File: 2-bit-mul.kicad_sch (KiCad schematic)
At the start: 3 parts, among them U6 74LS08, U7 74LS08, U8 74HC86

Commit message: feat(mul): clean version
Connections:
- net OUT_MUL_4 is gone; now on net OUT_MUL_3: U7.6
- net OUT_MUL_1: now also U8.3; no longer U6.6
- net OUT_MUL_2: now also U8.6; no longer U8.3
- net OUT_MUL_3: no longer U8.6
- removed net IN_A: U6.1, U6.10, U6.12, U6.13, U6.2, U6.4, U6.5, U6.9
- new net IN_A0: U6.1, U6.4
- new net IN_A1: U6.12, U6.9
- new net IN_B0: U6.13, U6.2
- new net IN_B1: U6.10, U6.5
- new net OUT_MUL_0: U6.6
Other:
- moved on the sheet: U6E, U7E, U8E
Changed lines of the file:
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@@
 		)
 	)
-	(hierarchical_label "OUT_MUL_3"
+	(hierarchical_label "OUT_MUL_2"
 		(shape output)
 		(at 132.08 73.66 0)
@@
 		)
 	)
-	(hierarchical_label "IN_A"
+	(hierarchical_label "IN_B0"
 		(shape input)
 		(at 53.34 99.06 180)
@@
 		)
 	)
-	(hierarchical_label "IN_A"
+	(hierarchical_label "IN_A0"
 		(shape input)
 		(at 54.61 40.64 180)
@@
 		)
 	)
-	(hierarchical_label "IN_A"
+	(hierarchical_label "IN_A1"
 		(shape input)
 		(at 54.61 46.99 180)
@@
 		)
 	)
-	(hierarchical_label "OUT_MUL_1"
+	(hierarchical_label "OUT_MUL_0"
 		(shape output)
 		(at 132.08 53.34 0)
@@
 		)
 	)
-	(hierarchical_label "OUT_MUL_2"
+	(hierarchical_label "OUT_MUL_1"
 		(shape output)
 		(at 132.08 63.5 0)
@@
 		)
 	)
-	(hierarchical_label "IN_A"
+	(hierarchical_label "IN_B1"
 		(shape input)
 		(at 53.34 87.63 180)
@@
 		)
 	)
-	(hierarchical_label "OUT_MUL_4"
+	(hierarchical_label "OUT_MUL_3"
 		(shape output)
 		(at 132.08 87.63 0)
@@
 		(on_board yes)
 		(dnp no)
-		(fields_autoplaced yes)
 		(property "Reference" "U6"
-			(at 74.9217 87.63 0)
+			(at 74.676 101.6 0)
 			(effects
 				(font
@@
 		)
 		(property "Value" "74LS08"
-			(at 74.9217 90.17 0)
+			(at 74.93 103.886 0)
 			(effects
 				(font
@@
 	(symbol
 		(lib_id "74xx:74LS08")
-		(at 97.79 119.38 0)
+		(at 96.52 129.54 0)
 		(unit 5)
 		(exclude_from_sim no)
@@
 		(fields_autoplaced yes)
 		(property "Reference" "U7"
-			(at 104.14 118.1099 0)
+			(at 102.87 128.2699 0)
 			(effects
 				(font
@@
 		)
 		(property "Value" "74LS08"
-			(at 104.14 120.6499 0)
+			(at 102.87 130.8099 0)
 			(effects
 				(font
@@
 		)
 		(property "Footprint" ""
-			(at 97.79 119.38 0)
+			(at 96.52 129.54 0)
 			(effects
 				(font
@@
 		)
 		(property "Datasheet" "http://www.ti.com/lit/gpn/sn74LS08"
-			(at 97.79 119.38 0)
+			(at 96.52 129.54 0)
 			(effects
 				(font
@@
 		)
 		(property "Description" "Quad And2"
-			(at 97.79 119.38 0)
+			(at 96.52 129.54 0)
 			(effects
 				(font
@@
 	(symbol
 		(lib_id "74xx:74LS08")
-		(at 74.93 119.38 0)
+		(at 73.66 129.54 0)
 		(unit 5)
 		(exclude_from_sim no)
@@
 		(fields_autoplaced yes)
 		(property "Reference" "U6"
-			(at 81.28 118.1099 0)
+			(at 80.01 128.2699 0)
 			(effects
 				(font
@@
 		)
 		(property "Value" "74LS08"
-			(at 81.28 120.6499 0)
+			(at 80.01 130.8099 0)
 			(effects
 				(font
@@
 		)
 		(property "Footprint" "Package_DIP:DIP-14_W7.62mm"
-			(at 74.93 119.38 0)
+			(at 73.66 129.54 0)
 			(effects
 				(font
@@
 		)
 		(property "Datasheet" "http://www.ti.com/lit/gpn/sn74LS08"
-			(at 74.93 119.38 0)
+			(at 73.66 129.54 0)
 			(effects
 				(font
@@
 		)
 		(property "Description" "Quad And2"
-			(at 74.93 119.38 0)
+			(at 73.66 129.54 0)
 			(effects
 				(font
@@
 		(dnp no)
 		(property "Reference" "U7"
-			(at 96.774 70.612 0)
+			(at 96.52 74.168 0)
 			(effects
 				(font
@@
 	(symbol
 		(lib_id "74xx:74HC86")
-		(at 120.65 118.11 0)
+		(at 119.38 128.27 0)
 		(unit 5)
 		(exclude_from_sim no)
@@
 		(fields_autoplaced yes)
 		(property "Reference" "U8"
-			(at 127 116.8399 0)
+			(at 125.73 126.9999 0)
 			(effects
 				(font
@@
 		)
 		(property "Value" "74HC86"
-			(at 127 119.3799 0)
+			(at 125.73 129.5399 0)
 			(effects
 				(font
@@
 		)
 		(property "Footprint" ""
-			(at 120.65 118.11 0)
+			(at 119.38 128.27 0)
 			(effects
 				(font
@@
 		)
 		(property "Datasheet" "http://www.ti.com/lit/gpn/sn74HC86"
-			(at 120.65 118.11 0)
+			(at 119.38 128.27 0)
 			(effects
 				(font
@@
 		)
 		(property "Description" "Quad 2-input XOR"
-			(at 120.65 118.11 0)
-			(effects
-				(font
+			(at 119.38 128.27 0)
+			(effects
+				(font

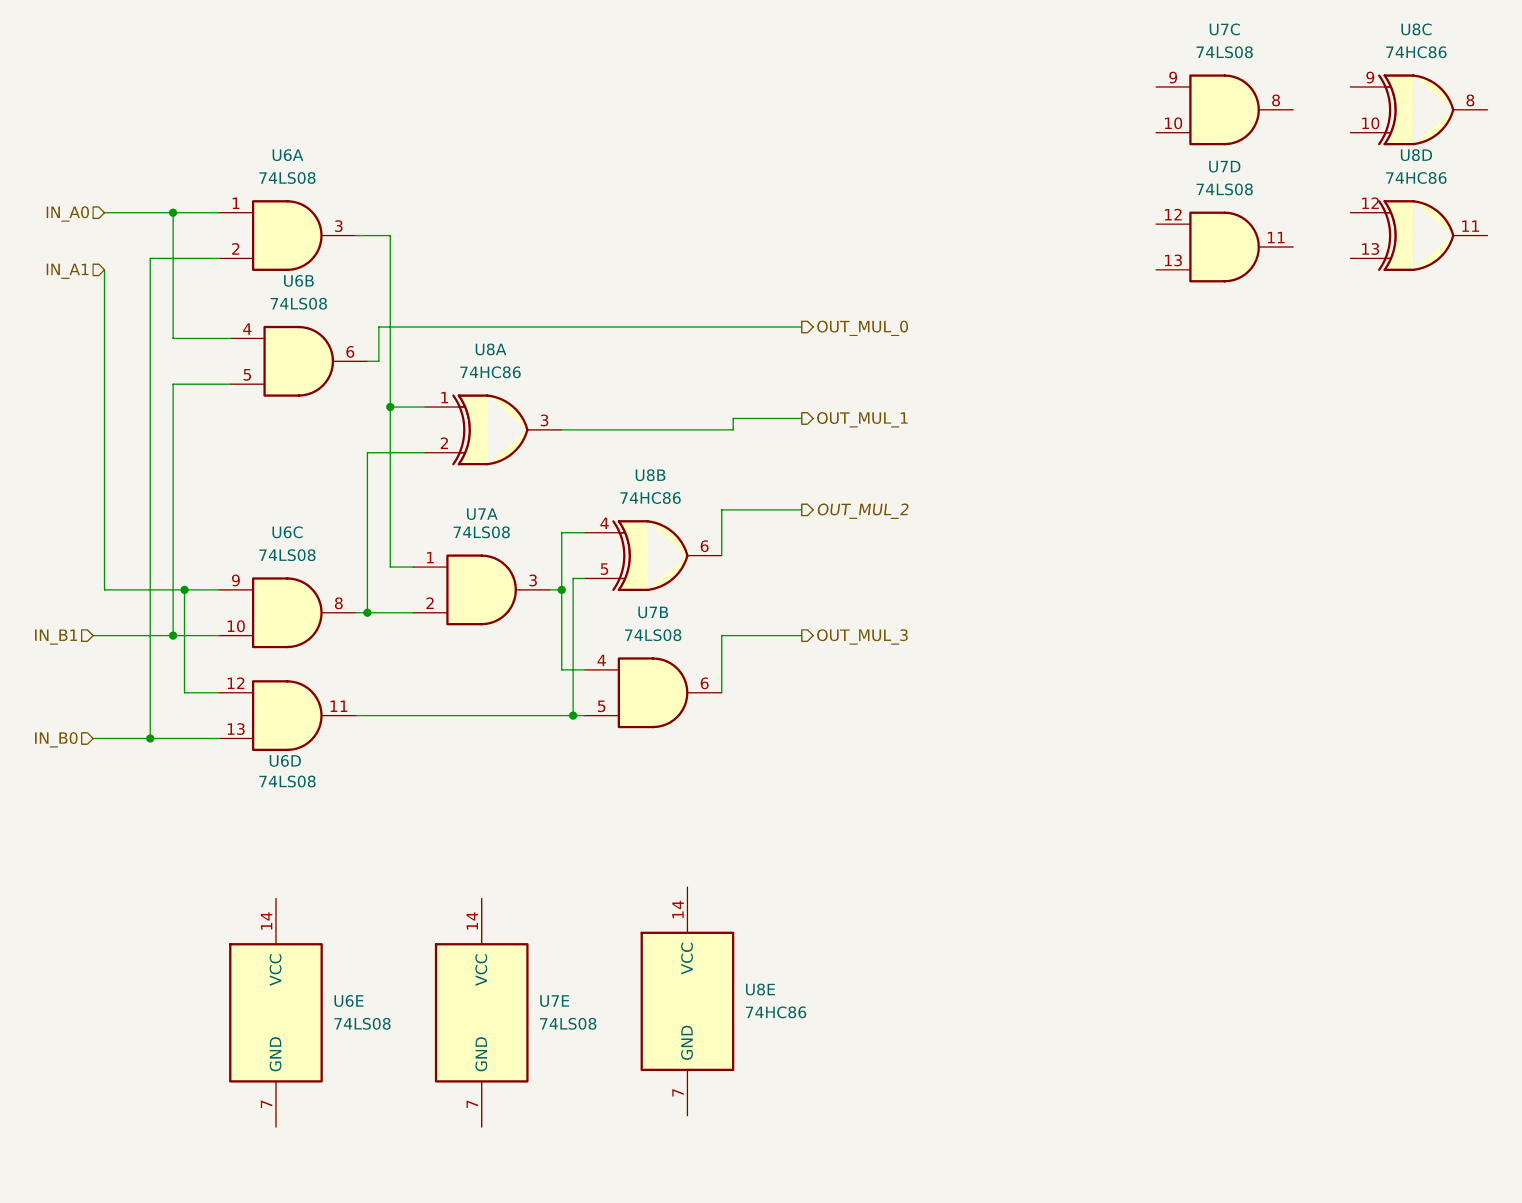
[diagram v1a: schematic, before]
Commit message: Add stuff and fix rce errors (#1)
* sync

* feat: removed ERC errors
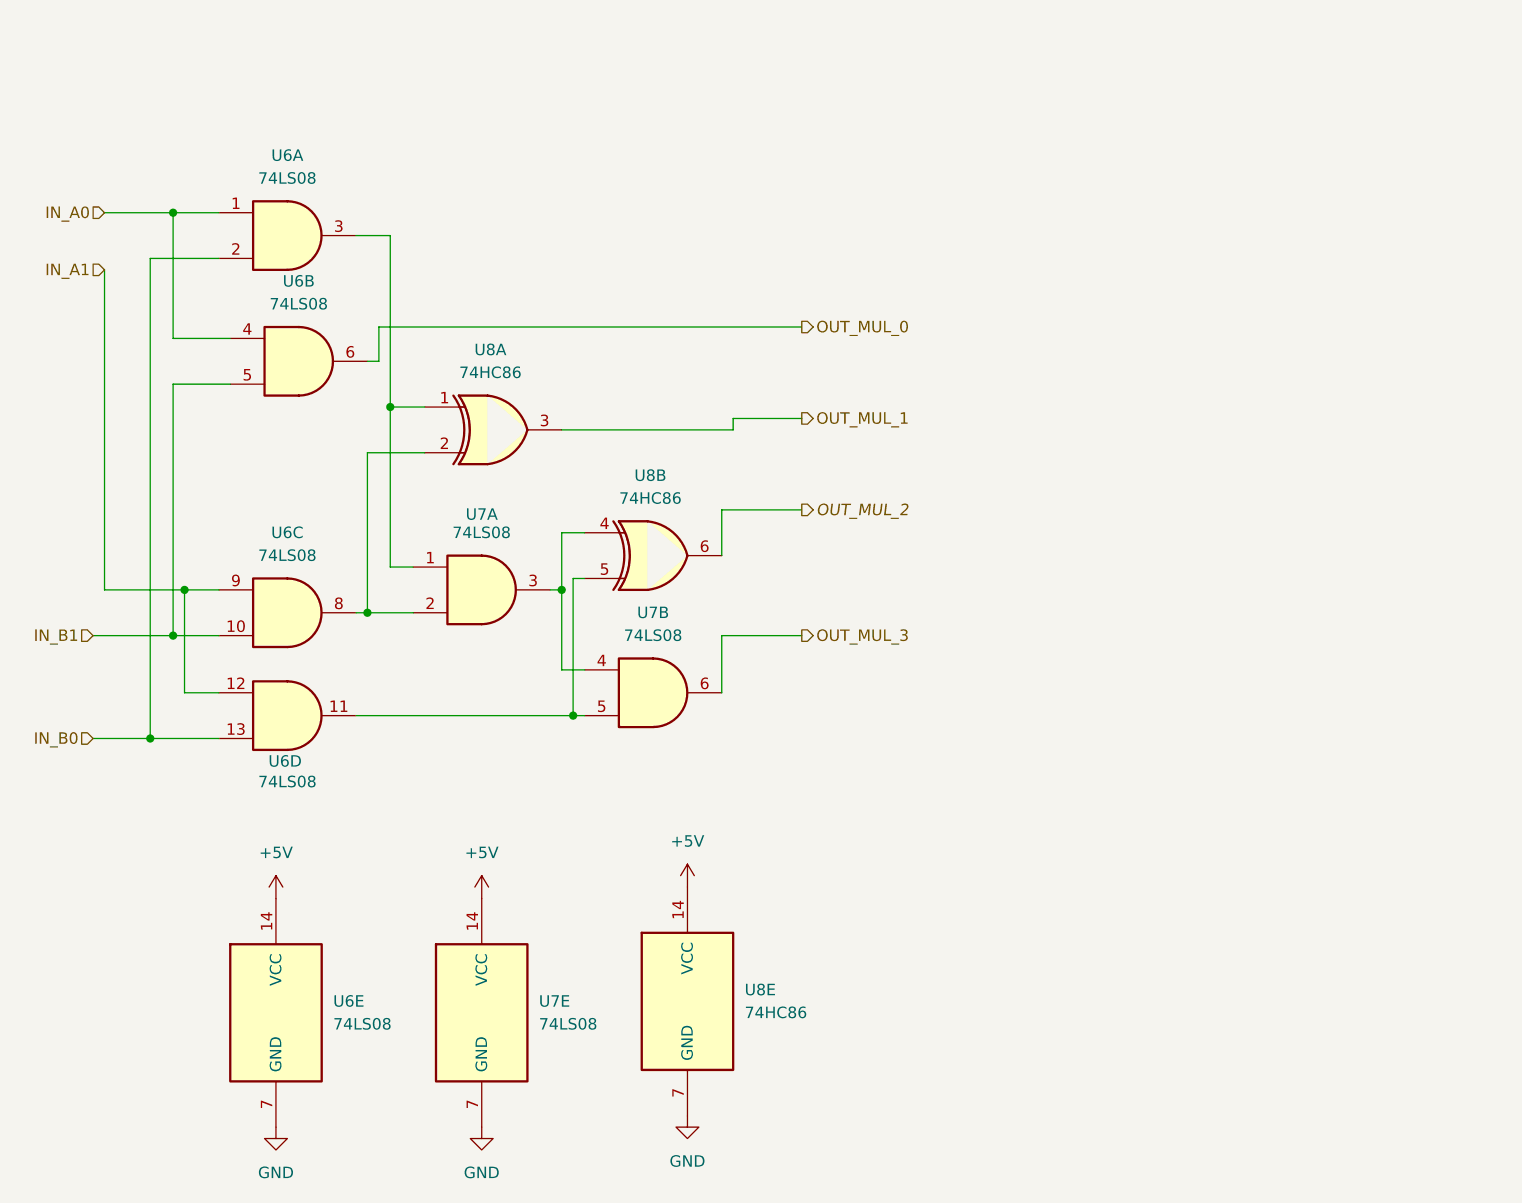
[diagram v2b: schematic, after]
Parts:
- removed unit 4 of U7
- removed unit 3 of U7
- removed unit 4 of U8
- removed unit 3 of U8
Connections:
- net +5V: now reaches U7.14 (VCC)
- net +5V: now also U6.14 (VCC), U8.14 (VCC)
- net GND: now reaches U7.7 (GND)
- net GND: now also U6.7 (GND), U8.7 (GND)

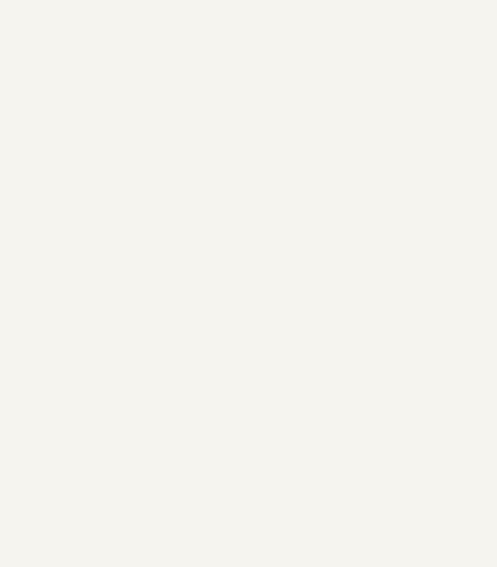
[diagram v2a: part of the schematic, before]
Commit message: fix: removed ERC warnings and errors
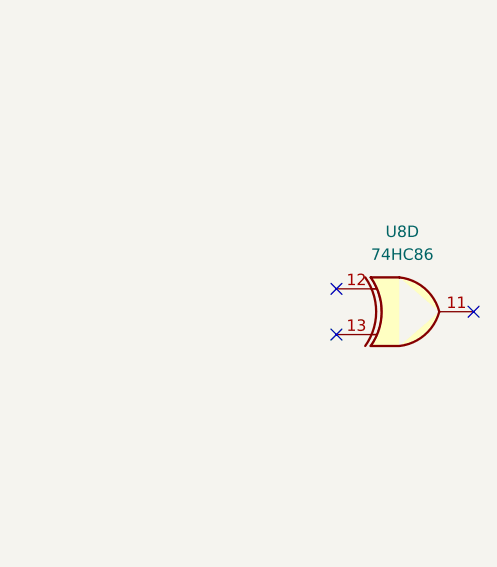
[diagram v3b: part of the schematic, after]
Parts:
- added unit 4 of U8
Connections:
- no-connect marks 0 -> 3
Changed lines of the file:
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@@
 		(color 0 0 0 0)
+	)
+	(no_connect
+		(at 194.31 88.9)
+	)
+	(no_connect
+		(at 209.55 86.36)
+	)
+	(no_connect
+		(at 194.31 83.82)
 	)
 	(wire
@@
 				)
 			)
+		)
+	)
+	(symbol
+		(lib_id "74xx:74HC86")
+		(at 201.93 86.36 0)
+		(unit 4)
+		(exclude_from_sim no)
+		(in_bom yes)
+		(on_board yes)
+		(dnp no)
+		(fields_autoplaced yes)
+		(property "Reference" "U8"
+			(at 201.6252 77.47 0)
+			(effects
+				(font
+					(size 1.27 1.27)
+				)
+			)
+		)
+		(property "Value" "74HC86"
+			(at 201.6252 80.01 0)
+			(effects
+				(font
+					(size 1.27 1.27)
+				)
+			)
+		)
+		(property "Footprint" ""
+			(at 201.93 86.36 0)
+			(effects
+				(font
+					(size 1.27 1.27)
+				)
+				(hide yes)
+			)
+		)
+		(property "Datasheet" "http://www.ti.com/lit/gpn/sn74HC86"
+			(at 201.93 86.36 0)
+			(effects
+				(font
+					(size 1.27 1.27)
+				)
+				(hide yes)
+			)
+		)
+		(property "Description" "Quad 2-input XOR"
+			(at 201.93 86.36 0)
+			(effects
+				(font
+					(size 1.27 1.27)
+				)
+				(hide yes)
+			)
+		)
+		(pin "10"
+		)
+		(pin "13"
+		)
+		(pin "8"
+		)
+		(pin "12"
+		)
+		(pin "9"
+		)
+		(pin "2"
+		)
+		(pin "1"
+		)
+		(pin "4"
+		)
+		(pin "3"
+		)
+		(pin "7"
+		)
+		(pin "14"
+		)
+		(pin "11"
+		)
+		(pin "6"
+		)
+		(pin "5"
+		)
+		(instances
+			(project "alu"
+				(path "/4987240f-8890-46b8-b8e9-0d60580cb205/aa82501c-f64e-4aae-993a-f2540e2bded8"
+					(reference "U8")
+					(unit 4)
+				)
+			)
